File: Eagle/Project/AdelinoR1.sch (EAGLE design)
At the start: 40 parts, among them J1 DC-044-A, J2 YELLOW-6P-2.54, J3 YELLOW-8P-2.54, J4 YELLOW-8P-2.54, J5 YELLOW-8P-2.54, J6 YELLOW-2X3P-2.54, J7 4P-2.0, J8 4P-2.0, Q1 NCE3407A, Q2 CJ2305, SW1 TS-1101F, U1 ATMEGA32U4-TQFP44, U2 CJT1117-5.0-SOT223, U4 CJT1117-3.3-SOT223, Y1 16MHZ

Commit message: ATmega32u4 wiring and some pinouts.
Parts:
- removed J6: YELLOW-2X3P-2.54, Seeed-Connector:DIP-YELLOW-MALE-HEADER-VERT(2X3P-2.54)
- removed SW1: TS-1101F, Seeed-Switch:DIP-BUTTON(2P-6.0X3.0X4.3MM)-TS-1101F
- removed Y1: 16MHZ, Seeed-Crystal Oscillator:SMD-CRYSTAL-16MHZ-8PF-20PPM-40R(2P-5.0X3.2MM)
- added C1, C2: 100nf, Seeed-Capacitor:CERAMIC-100NF-25V-10%-X7R(0402)
- added D1: 75V 150MA, Seeed-Diode:SMD-DIODE-SWITCHING-75V-150MA(D1206)
- added ICSP: YELLOW-2X3P-2.54, Seeed-Connector:DIP-YELLOW-MALE-HEADER-VERT(2X3P-2.54)
- added R4: 10K, Seeed-Resistor:SMD-RES-10K-1%-1/10W(0603)
- added R5: 1M, Seeed-Resistor:SMD-RES-1M-1%-1/10W(0603)
- added RESET_SW: TS-1101F, Seeed-Switch:DIP-BUTTON(2P-6.0X3.0X4.3MM)-TS-1101F
- added X1: 306010049_XTAL_16MHZ-3225_4P, Seeed-OPL-2017-01-Crystal-Akita:306010049_XTAL_16MHZ-3225_4P
- C10, C8: value 10pf -> 22pf; device Seeed-Capacitor:CERAMIC-10PF-50V-5%-NPO(0603) -> Seeed-Capacitor:CERAMIC-22PF-50V-5%-NPO(0603); NOTE ** CHECK VALUE ** -> (none)
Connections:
- new net N$11: J5.8
- new net N$12: J3.1
- new net N$13: J5.7
- new net N$14: J5.6
- new net N$15: J5.5
- new net N$16: J5.4
- new net N$17: J5.3
- new net N$18: J5.2
- new net N$19: J5.1
- new net N$20: J4.8
- new net N$21: J4.7
- new net N$22: J4.6
- new net N$23: J4.5
- new net N$24: J4.4
- new net N$25: J4.3
- new net N$26: J4.2
- new net N$27: J4.1
- new net N$28: J3.2
- new net N$29: J3.3
- new net N$30: J3.4
- new net N$31: J3.5
- new net N$32: J3.6
- new net N$33: J3.7
- new net N$34: J3.8
- new net N$35: J2.1
- new net N$36: J2.2
- new net N$37: J2.3
- new net N$38: J2.4
- new net N$39: J2.5
- new net N$40: J2.6
- new net N$41: ICSP.1
- new net N$42: ICSP.2
- new net N$43: U1.PE6(INT.6/AIN0)
- new net N$44: U1.PE2(!HWB)
- new net N$45: ICSP.5
- new net N$46: U1.PF0(ADC0)
- new net N$47: U1.PF1(ADC1)
- new net N$48: U1.PF4(ADC4/TCK)
- new net N$49: U1.PF5(ADC5/TMS)
- new net N$50: U1.PF6(ADC6/TDO)
- new net N$51: U1.PF7(ADC7/TDI)
- new net N$52: U1.PC6(OC3A/!OC4A)
- new net N$53: U1.PC7(ICP3/CLK0/OC4A)
- new net N$54: U1.PD0(OC0B/SCL/INT0)
- new net N$55: U1.PD1(SDA/INT1)
- new net N$56: U1.PD2(RXD1/INT2)
- new net N$57: U1.PD3(TXD1/INT3)
- new net N$58: U1.PD4(ICP1/ADC8)
- new net N$59: U1.PD5(XCLK1/!CTS)
- new net N$60: U1.PD6(T1/ADC9/!OC4D)
- new net N$61: U1.PD7(T0/OC4D/ADC10)
- new net N$62: U1.PB0(SS/PCINT0)
- new net N$63: U1.PB1(PCINT1/SCLK)
- new net N$64: U1.PB2(PDI/PCINT2/MOSI)
- new net N$65: U1.PB3(PD0/PCINT3/MISO)
- new net N$66: U1.PB4(PCINT4/ADC11)
- new net N$67: U1.PB5(PCINT5/OC1A/ADC12/!OC4B)
- new net N$68: U1.PB6(PCINT6/OC1B/OC4B/ADC13)
- new net N$69: U1.PB7(PCINT7/OC0A/OC1C/!RTS)
- new net RESET: D1.+, ICSP.3, R4.1, RESET_SW.2, U1.!RESET
- net +5V: now also C1.2, C2.2, D1.-, ICSP.6, R4.2
- net GND: now also C1.1, C2.1, ICSP.4, RESET_SW.1, X1.GND1, X1.GND2
- net N$5: now also R5.2, X1.P$1; no longer Y1.2
- net N$6: now also R5.1, X1.P$2; no longer Y1.1
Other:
- note added: "I/O PINS"
- moved on the sheet: C10, C3, C4, C5, C6, C7, C8, C9, J2, J3, J4, J5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

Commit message: Arduino-compatible pinout.
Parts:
- removed J7: 4P-2.0, Seeed-Connector:GROVE-CONNECTOR-DIP(4P-2.0)
- added I2C: 4P-2.0, Seeed-Connector:GROVE-CONNECTOR-DIP(4P-2.0)
- added L2: 330R-1500MA, Seeed-Inductor:SMD-FERRITE-BEAD-330R-1500MA(0805)'0805'
- U3: value (none) -> ESP-12F / OPL: 317060163 / SMD WIFI Module
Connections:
- net N$11 renamed PIN_AREF
- net N$59 renamed TXLED
- net N$62 renamed RXLED
- removed net N$13: J5.7
- removed net N$16: J5.4
- removed net N$17: J5.3
- removed net N$18: J5.2
- removed net N$19: J5.1
- removed net N$20: J4.8
- removed net N$21: J4.7
- removed net N$22: J4.6
- removed net N$23: J4.5
- removed net N$24: J4.4
- removed net N$25: J4.3
- removed net N$26: J4.2
- removed net N$27: J4.1
- removed net N$28: J3.2
- removed net N$29: J3.3
- removed net N$30: J3.4
- removed net N$31: J3.5
- removed net N$32: J3.6
- removed net N$33: J3.7
- removed net N$34: J3.8
- removed net N$35: J2.1
- removed net N$36: J2.2
- removed net N$37: J2.3
- removed net N$38: J2.4
- removed net N$39: J2.5
- removed net N$40: J2.6
- removed net N$41: ICSP.1
- removed net N$42: ICSP.2
- removed net N$43: U1.PE6(INT.6/AIN0)
- removed net N$45: ICSP.5
- removed net N$46: U1.PF0(ADC0)
- removed net N$47: U1.PF1(ADC1)
- removed net N$48: U1.PF4(ADC4/TCK)
- removed net N$49: U1.PF5(ADC5/TMS)
- removed net N$50: U1.PF6(ADC6/TDO)
- removed net N$51: U1.PF7(ADC7/TDI)
- removed net N$52: U1.PC6(OC3A/!OC4A)
- removed net N$53: U1.PC7(ICP3/CLK0/OC4A)
- removed net N$54: U1.PD0(OC0B/SCL/INT0)
- removed net N$55: U1.PD1(SDA/INT1)
- removed net N$56: U1.PD2(RXD1/INT2)
- removed net N$57: U1.PD3(TXD1/INT3)
- removed net N$58: U1.PD4(ICP1/ADC8)
- removed net N$60: U1.PD6(T1/ADC9/!OC4D)
- removed net N$61: U1.PD7(T0/OC4D/ADC10)
- removed net N$63: U1.PB1(PCINT1/SCLK)
- removed net N$64: U1.PB2(PDI/PCINT2/MOSI)
- removed net N$65: U1.PB3(PD0/PCINT3/MISO)
- removed net N$66: U1.PB4(PCINT4/ADC11)
- removed net N$67: U1.PB5(PCINT5/OC1A/ADC12/!OC4B)
- removed net N$68: U1.PB6(PCINT6/OC1B/OC4B/ADC13)
- removed net N$69: U1.PB7(PCINT7/OC0A/OC1C/!RTS)
- new net IOREF: J3.2, L2.2
- new net MISO: ICSP.1, U1.PB3(PD0/PCINT3/MISO)
- new net MOSI: ICSP.5, U1.PB2(PDI/PCINT2/MOSI)
- new net N$10: C11.2, C14.2, C15.2, Q1.S, U2.IN
- new net PIN_A0: J2.1, U1.PF7(ADC7/TDI)
- new net PIN_A1: J2.2, U1.PF6(ADC6/TDO)
- new net PIN_A2: J2.3, U1.PF5(ADC5/TMS)
- new net PIN_A3: J2.4, U1.PF4(ADC4/TCK)
- new net PIN_A4: J2.5, U1.PF1(ADC1)
- new net PIN_A5: J2.6, U1.PF0(ADC0)
- new net PIN_D0: J4.1, U1.PD2(RXD1/INT2)
- new net PIN_D1: J4.2, U1.PD3(TXD1/INT3)
- new net PIN_D10: J5.3, U1.PB6(PCINT6/OC1B/OC4B/ADC13)
- new net PIN_D11: J5.4, U1.PB7(PCINT7/OC0A/OC1C/!RTS)
- new net PIN_D12: J5.5, U1.PD6(T1/ADC9/!OC4D)
- new net PIN_D13: J5.6, U1.PC7(ICP3/CLK0/OC4A)
- new net PIN_D2: I2C.2, J4.3, U1.PD1(SDA/INT1)
- new net PIN_D3: I2C.1, J4.4, U1.PD0(OC0B/SCL/INT0)
- new net PIN_D4: J4.5, U1.PD4(ICP1/ADC8)
- new net PIN_D5: J4.6, U1.PC6(OC3A/!OC4A)
- new net PIN_D6: J4.7, U1.PD7(T0/OC4D/ADC10)
- new net PIN_D7: J4.8, U1.PE6(INT.6/AIN0)
- new net PIN_D8: J5.1, U1.PB4(PCINT4/ADC11)
- new net PIN_D9: J5.2, U1.PB5(PCINT5/OC1A/ADC12/!OC4B)
- new net SCK: ICSP.2, U1.PB1(PCINT1/SCLK)
- net +3V3: now also J3.4
- net +5V: now also I2C.3, J3.5, J8.3, L2.1
- net GND: now also I2C.4, J3.6, J3.7, J5.7, J8.4
- net N$14: now also J8.2; no longer J5.6
- net N$15: now also J8.1; no longer J5.5
- net RESET: now also J3.3
- net VIN: now also J3.8; no longer C11.2, C14.2, C15.2, Q1.S, U2.IN

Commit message: Add technical refs; ESP8266 wip.
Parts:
- added R6, R7, R8: 10K, Seeed-Resistor:SMD-RES-10K-1%-1/10W(0603)
- renumbered J8 to DIO1
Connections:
- removed net N$12: J3.1
- removed net N$14: DIO1.2
- removed net N$15: DIO1.1
- removed net N$4: C7.1, U1.AREF
- new net GPIO0: U3.GPIO0
- new net GPIO15: R6.2, U3.GPIO15
- new net GPIO2: R8.2, U3.GPIO2
- new net N$11: U3.GPIO4
- new net N$13: U3.GPIO5
- net +3V3: now also R8.1, U3.VCC
- net GND: now also R6.1, U3.GND
- net PIN_AREF: now also C7.1, U1.AREF
- net PIN_D0: now also U3.TXD
- net PIN_D1: now also U3.RXD
- net PIN_D10: now also DIO1.1
- net PIN_D9: now also DIO1.2
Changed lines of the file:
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@@
 <part name="J1" library="Seeed-Connector" deviceset="JACK-DC-044-A" device="" value="DC-044-A"/>
 <part name="I2C" library="Seeed-Connector" deviceset="GROVE-CONNECTOR-DIP(4P-2.0)" device="" value="4P-2.0"/>
-<part name="J8" library="Seeed-Connector" deviceset="GROVE-CONNECTOR-DIP(4P-2.0)" device="" value="4P-2.0"/>
+<part name="DIO1" library="Seeed-Connector" deviceset="GROVE-CONNECTOR-DIP(4P-2.0)" device="" value="4P-2.0"/>
 <part name="GND1" library="supply1" library_urn="urn:adsk.eagle:library:371" deviceset="GND" device=""/>
 <part name="R1" library="Seeed-Resistor" deviceset="SMD-RES-22R-5%-1/10W(0603)" device="" value="22R"/>
@@
 <part name="R5" library="Seeed-Resistor" deviceset="SMD-RES-1M-1%-1/10W(0603)" device="" value="1M"/>
 <part name="L2" library="Seeed-Inductor" deviceset="SMD-FERRITE-BEAD-330R-1500MA(0805)" device="'0805'" value="330R-1500MA"/>
+<part name="+3V2" library="supply1" library_urn="urn:adsk.eagle:library:371" deviceset="+3V3" device=""/>
+<part name="GND11" library="supply1" library_urn="urn:adsk.eagle:library:371" deviceset="GND" device=""/>
+<part name="R6" library="Seeed-Resistor" deviceset="SMD-RES-10K-1%-1/10W(0603)" device="" value="10K"/>
+<part name="R7" library="Seeed-Resistor" deviceset="SMD-RES-10K-1%-1/10W(0603)" device="" value="10K"/>
+<part name="R8" library="Seeed-Resistor" deviceset="SMD-RES-10K-1%-1/10W(0603)" device="" value="10K"/>
+<part name="+3V3" library="supply1" library_urn="urn:adsk.eagle:library:371" deviceset="+3V3" device=""/>
+<part name="GND12" library="supply1" library_urn="urn:adsk.eagle:library:371" deviceset="GND" device=""/>
 </parts>
 <sheets>
@@
 <instance part="J1" gate="G$1" x="-219.71" y="67.31"/>
 <instance part="I2C" gate="G$1" x="-85.09" y="-113.03"/>
-<instance part="J8" gate="G$1" x="-52.07" y="-113.03"/>
+<instance part="DIO1" gate="G$1" x="-52.07" y="-113.03"/>
 <instance part="GND1" gate="1" x="-222.25" y="121.92"/>
 <instance part="R1" gate="G$1" x="-170.18" y="142.24" smashed="yes">
@@
 </instance>
 <instance part="L2" gate="L" x="-130.81" y="76.2"/>
+<instance part="+3V2" gate="G$1" x="101.6" y="-73.66" rot="R90"/>
+<instance part="GND11" gate="1" x="102.87" y="-82.55"/>
+<instance part="R6" gate="G$1" x="71.12" y="-118.11" smashed="yes">
+<attribute name="NAME" x="67.31" y="-116.84" size="1.27" layer="95" ratio="10"/>
+<attribute name="VALUE" x="72.39" y="-116.84" size="1.27" layer="96" ratio="10"/>
+</instance>
+<instance part="R7" gate="G$1" x="74.93" y="-78.74"/>
+<instance part="R8" gate="G$1" x="71.12" y="-113.03" smashed="yes">
+<attribute name="NAME" x="67.31" y="-111.76" size="1.27" layer="95" ratio="10"/>
+<attribute name="VALUE" x="72.39" y="-111.76" size="1.27" layer="96" ratio="10"/>
+</instance>
+<instance part="+3V3" gate="G$1" x="62.23" y="-107.95" smashed="yes">
+<attribute name="VALUE" x="58.42" y="-106.68" size="1.778" layer="96"/>
+</instance>
+<instance part="GND12" gate="1" x="62.23" y="-123.19"/>
 </instances>
 <busses>
@@
 </segment>
 <segment>
-<pinref part="J8" gate="G$1" pin="4"/>
+<pinref part="DIO1" gate="G$1" pin="4"/>
 <wire x1="-55.88" y1="-116.84" x2="-66.04" y2="-116.84" width="0.1524" layer="91"/>
 <label x="-66.04" y="-118.11" size="1.4224" layer="95"/>
+</segment>
+<segment>
+<pinref part="U3" gate="G$1" pin="GND"/>
+<pinref part="GND11" gate="1" pin="GND"/>
+<wire x1="115.57" y1="-78.74" x2="102.87" y2="-78.74" width="0.1524" layer="91"/>
+<wire x1="102.87" y1="-78.74" x2="102.87" y2="-80.01" width="0.1524" layer="91"/>
+</segment>
+<segment>
+<pinref part="GND12" gate="1" pin="GND"/>
+<pinref part="R6" gate="G$1" pin="1"/>
+<wire x1="62.23" y1="-120.65" x2="62.23" y2="-118.11" width="0.1524" layer="91"/>
+<wire x1="62.23" y1="-118.11" x2="67.31" y2="-118.11" width="0.1524" layer="91"/>
 </segment>
 </net>
@@
 <wire x1="-210.82" y1="-95.25" x2="-223.52" y2="-95.25" width="0.1524" layer="91"/>
 <label x="-223.52" y="-96.52" size="1.27" layer="95"/>
-</segment>
-</net>
-<net name="N$4" class="0">
-<segment>
-<pinref part="U1" gate="G$1" pin="AREF"/>
-<pinref part="C7" gate="G$1" pin="1"/>
-<wire x1="106.68" y1="113.03" x2="97.79" y2="113.03" width="0.1524" layer="91"/>
 </segment>
 </net>
@@
 </segment>
 <segment>
-<pinref part="J8" gate="G$1" pin="3"/>
+<pinref part="DIO1" gate="G$1" pin="3"/>
 <wire x1="-55.88" y1="-114.3" x2="-66.04" y2="-114.3" width="0.1524" layer="91"/>
 <label x="-66.04" y="-115.57" size="1.4224" layer="95"/>
@@
 <wire x1="-210.82" y1="-85.09" x2="-223.52" y2="-85.09" width="0.1524" layer="91"/>
 <label x="-223.52" y="-86.36" size="1.27" layer="95"/>
+</segment>
+<segment>
+<pinref part="U3" gate="G$1" pin="VCC"/>
+<pinref part="+3V2" gate="G$1" pin="+3V3"/>
+<wire x1="115.57" y1="-73.66" x2="104.14" y2="-73.66" width="0.1524" layer="91"/>
+</segment>
+<segment>
+<pinref part="+3V3" gate="G$1" pin="+3V3"/>
+<pinref part="R8" gate="G$1" pin="1"/>
+<wire x1="62.23" y1="-110.49" x2="62.23" y2="-113.03" width="0.1524" layer="91"/>
+<wire x1="62.23" y1="-113.03" x2="67.31" y2="-113.03" width="0.1524" layer="91"/>
 </segment>
 </net>
@@
 <label x="-134.62" y="-72.39" size="1.4224" layer="95" rot="R180"/>
 </segment>
-</net>
-<net name="N$12" class="0">
-<segment>
-<pinref part="J3" gate="G$1" pin="1"/>
-<wire x1="-210.82" y1="-77.47" x2="-223.52" y2="-77.47" width="0.1524" layer="91"/>
+<segment>
+<pinref part="U1" gate="G$1" pin="AREF"/>
+<pinref part="C7" gate="G$1" pin="1"/>
+<wire x1="106.68" y1="113.03" x2="102.87" y2="113.03" width="0.1524" layer="91"/>
+<wire x1="102.87" y1="113.03" x2="97.79" y2="113.03" width="0.1524" layer="91"/>
+<wire x1="102.87" y1="113.03" x2="102.87" y2="107.95" width="0.1524" layer="91"/>
+<junction x="102.87" y="113.03"/>
+<wire x1="102.87" y1="107.95" x2="93.98" y2="107.95" width="0.1524" layer="91"/>
+<label x="93.98" y="107.95" size="1.4224" layer="95"/>
 </segment>
 </net>
@@
 <label x="182.88" y="57.15" size="1.4224" layer="95" rot="R180"/>
 </segment>
+<segment>
+<pinref part="DIO1" gate="G$1" pin="1"/>
+<wire x1="-55.88" y1="-109.22" x2="-66.04" y2="-109.22" width="0.1524" layer="91"/>
+<label x="-66.04" y="-110.49" size="1.4224" layer="95"/>
+</segment>
 </net>
 <net name="PIN_D9" class="0">
@@
 <label x="182.88" y="59.69" size="1.4224" layer="95" rot="R180"/>
 </segment>
+<segment>
+<pinref part="DIO1" gate="G$1" pin="2"/>
+<wire x1="-55.88" y1="-111.76" x2="-66.04" y2="-111.76" width="0.1524" layer="91"/>
+<label x="-66.04" y="-113.03" size="1.4224" layer="95"/>
+</segment>
 </net>
 <net name="PIN_D8" class="0">
@@
 <label x="182.88" y="90.17" size="1.4224" layer="95" rot="R180"/>
 </segment>
+<segment>
+<pinref part="U3" gate="G$1" pin="RXD"/>
+<wire x1="151.13" y1="-68.58" x2="161.29" y2="-68.58" width="0.1524" layer="91"/>
+<label x="161.29" y="-68.58" size="1.4224" layer="95" rot="R180"/>
+</segment>
 </net>
 <net name="PIN_D0" class="0">
@@
 <label x="182.88" y="92.71" size="1.4224" layer="95" rot="R180"/>
 </segment>
+<segment>
+<pinref part="U3" gate="G$1" pin="TXD"/>
+<wire x1="151.13" y1="-66.04" x2="161.29" y2="-66.04" width="0.1524" layer="91"/>
+<label x="161.29" y="-66.04" size="1.4224" layer="95" rot="R180"/>
+</segment>
 </net>
 <net name="PIN_A0" class="0">
@@
 <pinref part="U1" gate="G$1" pin="PF0(ADC0)"/>
 <wire x1="170.18" y1="125.73" x2="182.88" y2="125.73" width="0.1524" layer="91"/>
-<label x="182.88" y="125.73" size="1.27" layer="95" rot="R180"/>
+<label x="182.88" y="125.73" size="1.4224" layer="95" rot="R180"/>
 </segment>
 </net>
@@
 </segment>
 </net>
-<net name="N$14" class="0">
-<segment>
-<pinref part="J8" gate="G$1" pin="2"/>
-<wire x1="-55.88" y1="-111.76" x2="-66.04" y2="-111.76" width="0.1524" layer="91"/>
-<label x="-66.04" y="-113.03" size="1.4224" layer="95"/>
-</segment>
-</net>
-<net name="N$15" class="0">
-<segment>
-<pinref part="J8" gate="G$1" pin="1"/>
-<wire x1="-55.88" y1="-109.22" x2="-66.04" y2="-109.22" width="0.1524" layer="91"/>
-<label x="-66.04" y="-110.49" size="1.4224" layer="95"/>
-</segment>
-</net>
+<net name="N$11" class="0">
+<segment>
+<pinref part="U3" gate="G$1" pin="GPIO4"/>
+<wire x1="151.13" y1="-78.74" x2="161.29" y2="-78.74" width="0.1524" layer="91"/>
+</segment>
+</net>
+<net name="N$13" class="0">
+<segment>
+<pinref part="U3" gate="G$1" pin="GPIO5"/>
+<wire x1="151.13" y1="-81.28" x2="161.29" y2="-81.28" width="0.1524" layer="91"/>
+</segment>
+</net>
+<net name="GPIO0" class="0">
+<segment>
+<pinref part="U3" gate="G$1" pin="GPIO0"/>
+<wire x1="151.13" y1="-73.66" x2="161.29" y2="-73.66" width="0.1524" layer="91"/>
+<label x="161.29" y="-73.66" size="1.4224" layer="95" rot="R180"/>
+</segment>
+</net>
+<net name="GPIO2" class="0">
+<segment>
+<pinref part="U3" gate="G$1" pin="GPIO2"/>
+<wire x1="151.13" y1="-76.2" x2="161.29" y2="-76.2" width="0.1524" layer="91"/>
+<label x="161.29" y="-76.2" size="1.4224" layer="95" rot="R180"/>
+</segment>
+<segment>
+<pinref part="R8" gate="G$1" pin="2"/>
+<wire x1="74.93" y1="-113.03" x2="85.09" y2="-113.03" width="0.1524" layer="91"/>
+<label x="85.09" y="-113.03" size="1.4224" layer="95" rot="R180"/>
+</segment>
+</net>
+<net name="GPIO15" class="0">
+<segment>
+<pinref part="U3" gate="G$1" pin="GPIO15"/>
+<wire x1="115.57" y1="-99.06" x2="105.41" y2="-99.06" width="0.1524" layer="91"/>
+<label x="105.41" y="-99.06" size="1.4224" layer="95"/>
+</segment>
+<segment>
+<pinref part="R6" gate="G$1" pin="2"/>
+<wire x1="74.93" y1="-118.11" x2="85.09" y2="-118.11" width="0.1524" layer="91"/>
+<label x="85.09" y="-118.11" size="1.4224" layer="95" rot="R180"/>
+</segment>
+</net>

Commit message: Base circuit finished; ERC pass.
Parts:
- removed L2: 330R-1500MA, Seeed-Inductor:SMD-FERRITE-BEAD-330R-1500MA(0805)'0805'
- added D4: GRE-0603, Seeed-LED:SMD-LED-CLEAR-GREEN(0603)
- added D5, D6: YEL-0603, Seeed-LED:SMD-LED-CLEAR-YELLOW(0603)
- added R10, R11, R12, R13, R14, R15, R16, R9: 1K, Seeed-Resistor:SMD-RES-1K-1%-1/10W(0603)
- R8: value 10K -> 1K; device Seeed-Resistor:SMD-RES-10K-1%-1/10W(0603) -> Seeed-Resistor:SMD-RES-1K-1%-1/10W(0603)
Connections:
- net GPIO15 renamed N$4
- removed net GPIO0: U3.GPIO0
- removed net GPIO2: R8.2, U3.GPIO2
- removed net IOREF: J3.2, L2.2
- removed net N$13: U3.GPIO5
- removed net N$44: U1.PE2(!HWB)
- new net ESP_EN: R10.1, U1.PE2(!HWB), U3.EN
- new net N$14: R13.2, U3.RST
- new net N$15: R11.1, R7.1, U3.GPIO0
- new net N$16: D4.+, R12.2
- new net N$17: R15.1, U3.TXD
- new net N$18: R14.1, U3.RXD
- new net N$19: D5.+, R9.2
- new net N$20: D6.+, R8.2
- net +3V3: now also R16.2, R7.2; no longer R8.1
- net +5V: now also J3.2, R12.1, R8.1, R9.1; no longer L2.1
- net GND: now also D4.-, R10.2
- net MOSI: now also R11.2
- net N$11: now also R16.1, U3.GPIO2; no longer U3.GPIO4
- net PIN_D0: now also R15.2; no longer U3.TXD
- net PIN_D1: now also R14.2; no longer U3.RXD
- net PIN_D2: now also U3.GPIO5
- net PIN_D3: now also U3.GPIO4
- net RXLED: now also D5.-
- net SCK: now also R13.1
- net TXLED: now also D6.-
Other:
- moved on the sheet: C1, C10, C2, C3, C4, C5, C6, C7, C8, C9, D1, R4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

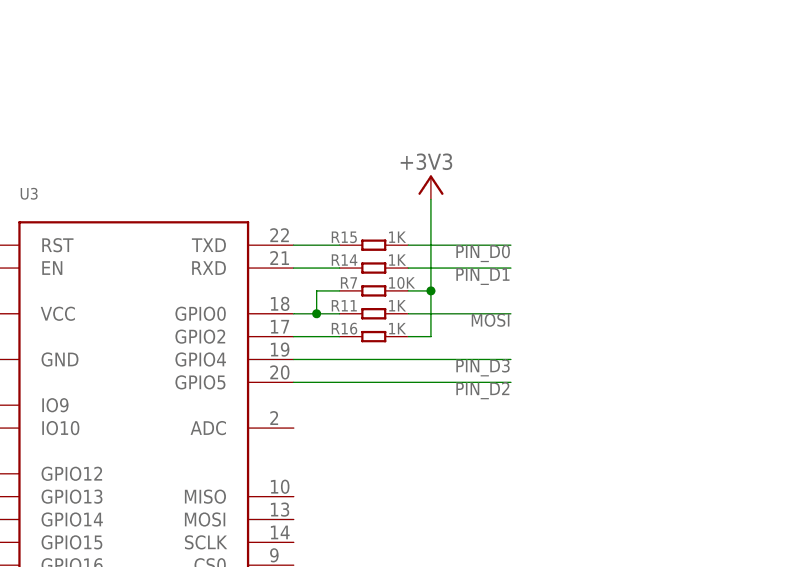
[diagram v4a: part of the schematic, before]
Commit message: Fix R7 too strong pull-up for GPIO0.
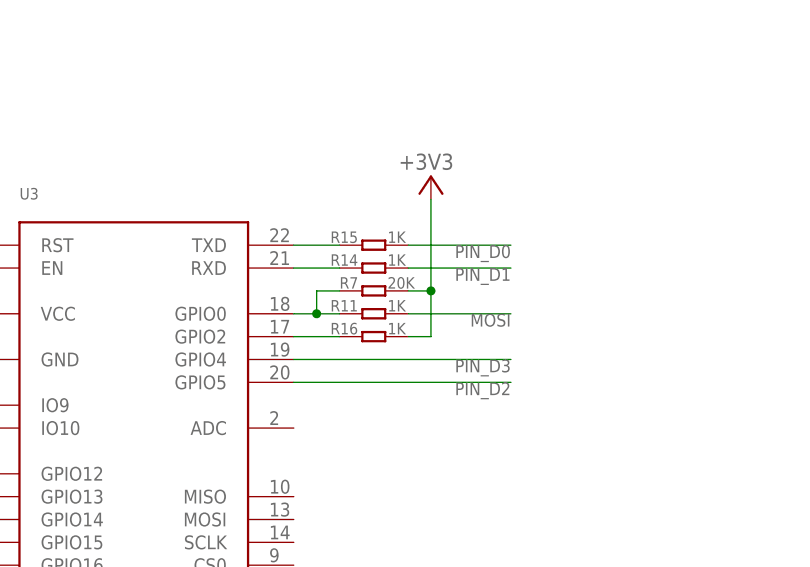
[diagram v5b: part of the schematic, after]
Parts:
- R7: value 10K -> 20K; device Seeed-Resistor:SMD-RES-10K-1%-1/10W(0603) -> Seeed-Resistor:SMD-RES-20K-1%-1/10W(0603)
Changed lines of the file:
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@@
 <part name="R16" library="Seeed-Resistor" deviceset="SMD-RES-1K-1%-1/10W(0603)" device="" value="1K"/>
 <part name="+3V4" library="supply1" library_urn="urn:adsk.eagle:library:371" deviceset="+3V3" device=""/>
-<part name="R7" library="Seeed-Resistor" deviceset="SMD-RES-10K-1%-1/10W(0603)" device="" value="10K"/>
+<part name="R7" library="Seeed-Resistor" deviceset="SMD-RES-20K-1%-1/10W(0603)" device="" value="20K"/>
 <part name="R8" library="Seeed-Resistor" deviceset="SMD-RES-1K-1%-1/10W(0603)" device="" value="1K"/>
 <part name="R9" library="Seeed-Resistor" deviceset="SMD-RES-1K-1%-1/10W(0603)" device="" value="1K"/>
